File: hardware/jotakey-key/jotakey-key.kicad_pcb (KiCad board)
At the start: 2 copper layers, 18 x 47 mm, 27 parts, among them J1 USB_A_PCB_Edge, U1 STM32L432KCU6, U2 SLS32AIA010MH, U3 XC6206P332MR, U4 USBLC6-2SC6

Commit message: hardware: label the SWD pads, set the board finish
The five SWD test pads on the bottom get their signals in silkscreen
(DIO, CLK, RST, 3V3, GND), 0.8 mm high under each pad, placed by silk.py
from the test-point positions.

The stackup now records ENIG and a bevelled edge connector (set in
Board Setup > Board Finish), as HARDWARE.md specifies. The silkscreen
bolt on the touch electrode, lost when E1 was updated from a stale copy
of the library, is back. DRC: no violations.

Co-Authored-By: Claude Opus 5.5 <noreply@anthropic.com>
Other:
- board text added: "3V3"
- board text added: "CLK"
- board text added: "DIO"
- board text added: "GND"
- board text added: "RST"
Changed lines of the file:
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@@
 			(layer "F.SilkS"
 				(type "Top Silk Screen")
-				(color "White")
 			)
 			(layer "F.Paste"
@@
 			(layer "B.SilkS"
 				(type "Bottom Silk Screen")
-				(color "White")
 			)
-			(copper_finish "None")
+			(copper_finish "ENIG")
 			(dielectric_constraints no)
+			(edge_connector bevelled)
 		)
 		(pad_to_mask_clearance 0.05)
@@
 		(attr smd)
 		(duplicate_pad_numbers_are_jumpers no)
+		(fp_poly
+			(pts
+				(xy 0.3182 -3.5) (xy -2.5455 0.3182) (xy -0.6364 0.3182) (xy -1.9091 3.5) (xy 2.5455 -0.6364) (xy 0.3182 -0.6364)
+				(xy 2.2273 -3.5)
+			)
+			(stroke
+				(width 0)
+				(type solid)
+			)
+			(fill yes)
+			(layer "F.SilkS")
+		)
 		(fp_circle
 			(center 0 0)
@@
 		)
 		(embedded_fonts no)
-		(fp_poly (pts (xy 0.3182 -3.5000) (xy -2.5455 0.3182) (xy -0.6364 0.3182) (xy -1.9091 3.5000) (xy 2.5455 -0.6364) (xy 0.3182 -0.6364) (xy 2.2273 -3.5000)) (stroke (width 0) (type solid)) (fill yes) (layer "F.SilkS"))
 	)
 	(footprint "Capacitor_SMD:C_0402_1005Metric"
@@
 		)
 	)
+	(gr_text "DIO"
+		(at 94.92 99.65 0)
+		(layer "B.SilkS")
+		(effects
+			(font
+				(size 0.8 0.8)
+				(thickness 0.12)
+			)
+			(justify mirror)
+		)
+	)
+	(gr_text "CLK"
+		(at 97.46 99.65 0)
+		(layer "B.SilkS")
+		(effects
+			(font
+				(size 0.8 0.8)
+				(thickness 0.12)
+			)
+			(justify mirror)
+		)
+	)
+	(gr_text "RST"
+		(at 100 99.65 0)
+		(layer "B.SilkS")
+		(effects
+			(font
+				(size 0.8 0.8)
+				(thickness 0.12)
+			)
+			(justify mirror)
+		)
+	)
+	(gr_text "3V3"
+		(at 102.54 99.65 0)
+		(layer "B.SilkS")
+		(effects
+			(font
+				(size 0.8 0.8)
+				(thickness 0.12)
+			)
+			(justify mirror)
+		)
+	)
+	(gr_text "GND"
+		(at 105.08 99.65 0)
+		(layer "B.SilkS")
+		(effects
+			(font
+				(size 0.8 0.8)
+				(thickness 0.12)
+			)
+			(justify mirror)
+		)
+	)

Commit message: hardware: label the chips with their function
MCU, OPTIGA, LDO and ESD on the top silkscreen, 0.8 mm high, each in the
free space nearest its chip and clear of pads and pin-1 marks; silk.py
places them relative to the footprints. DRC: no violations.

Co-Authored-By: Claude Opus 5.5 <noreply@anthropic.com>
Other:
- board text added: "ESD"
- board text added: "LDO"
- board text added: "MCU"
- board text added: "OPTIGA"
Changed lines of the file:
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@@
+		)
+	)
+	(gr_text "LDO"
+		(at 95.5 82.95 0)
+		(layer "F.SilkS")
+		(effects
+			(font
+				(size 0.8 0.8)
+				(thickness 0.15)
+			)
+		)
+	)
+	(gr_text "ESD"
+		(at 100 87.6 0)
+		(layer "F.SilkS")
+		(effects
+			(font
+				(size 0.8 0.8)
+				(thickness 0.15)
+			)
+		)
+	)
+	(gr_text "MCU"
+		(at 100 99.5 0)
+		(layer "F.SilkS")
+		(effects
+			(font
+				(size 0.8 0.8)
+				(thickness 0.15)
+			)
+		)
+	)
+	(gr_text "OPTIGA"
+		(at 106.2 83 0)
+		(layer "F.SilkS")
+		(effects
+			(font
+				(size 0.8 0.8)
+				(thickness 0.15)
+			)
 		)
 	)

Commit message: Copyright notices, a release workflow, and nothing third-party
- (c) Javier Fernandez @ JotaSoft 2026 at the top of every source file
  (Rust, Lean, Python, Typst, shell), in the report's cover and page
  footers, on the board's bottom silkscreen, in the schematic and PCB
  title blocks, as the Cargo authors, and in a new README.
- .github/workflows/release.yml: on every hw-v*/fw-v* tag, build the
  report in its screen and print versions with a pinned Typst, keep both
  as workflow artifacts, and attach them to the tag's GitHub release.
- docs/fonts: the report's fonts (SIL OFL, and Bitstream Vera for the
  math font) with their licences, so local and CI builds match; the doc
  recipes build with them only.
- Third-party documents (datasheets, specifications, papers) are no
  longer tracked; their README indexes keep every source link.

Co-Authored-By: Claude Opus 5.5 <noreply@anthropic.com>
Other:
- board text added: "(c) Javier Fernandez @ JotaSoft 2026"
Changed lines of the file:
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@@
 		(comment 1 "Pin plan and parts: hardware/HARDWARE.md")
 		(comment 2 "Fabrication and assembly: JLCPCB, 2 layers, 2.0 mm, ENIG")
+		(comment 3 "(c) Javier Fernandez @ JotaSoft 2026")
 	)
 	(layers
@@
 			)
 			(justify mirror)
+		)
+	)
+	(gr_text "(c) Javier Fernandez\n@ JotaSoft 2026"
+		(at 100 110.6 0)
+		(layer "B.SilkS")
+		(effects
+			(font
+				(size 0.8 0.8)
+				(thickness 0.15)
+			)
+			(justify mirror)

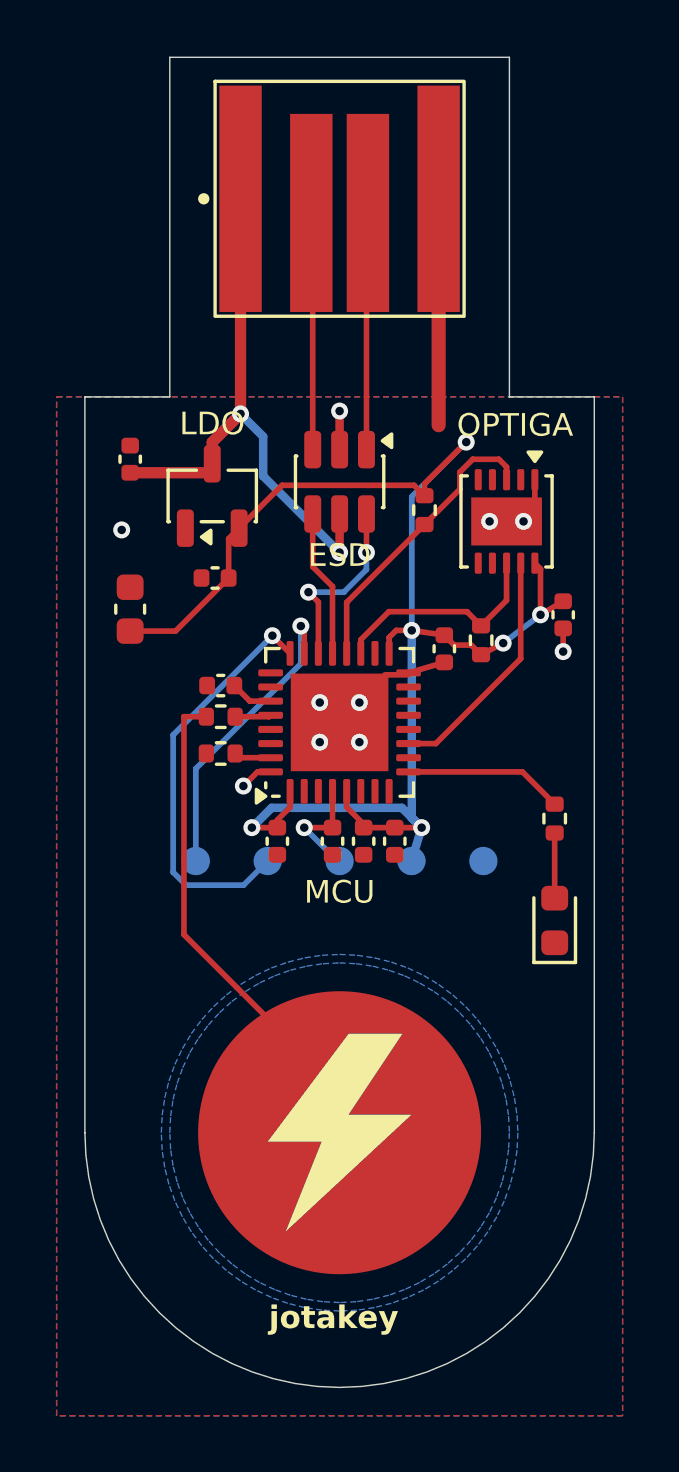
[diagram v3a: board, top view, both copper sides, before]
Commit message: hw: 0R bring-up links R6, R7; hardware 0.2.0
Split the 3.3 V supply into +3V3 (LDO), +3V3_MCU (via R6) and
+3V3_SE (via R7) so a hand-built board can be brought up one stage at
a time. The I2C pull-ups move to the OPTIGA's rail so they cannot
back-power it while R7 is open.

Board: R6 between the LDO and U4, R7 beside U4, R3 0.4 mm right, the
SE rail over U2 and down the edge to C9, a GND via to stitch the top
pour. ERC, DRC and schematic parity clean. HARDWARE.md, MANUFACTURING.md
(staged bring-up), README, chapter 7, renders and PDFs updated.

Co-Authored-By: Claude Opus 5.5 <noreply@anthropic.com>
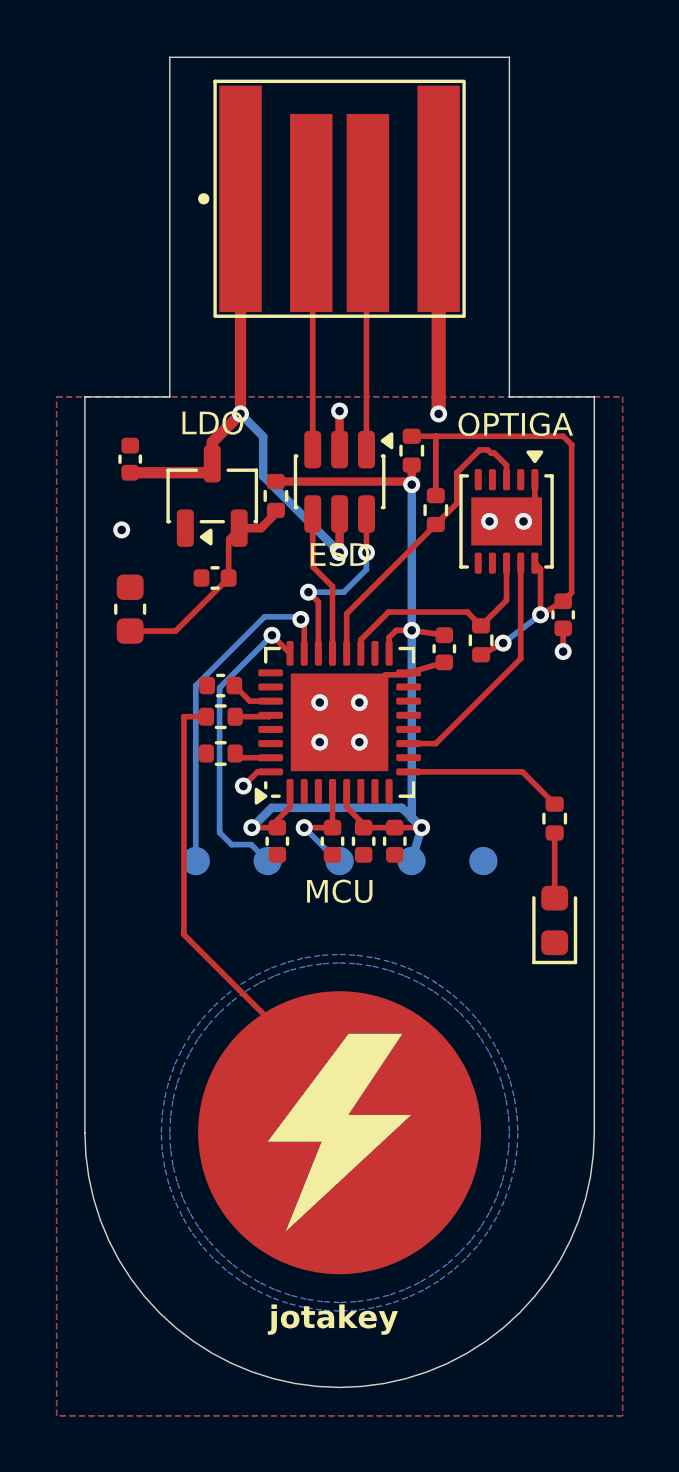
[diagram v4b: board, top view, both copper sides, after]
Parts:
- added R6: 0R, Resistor_SMD:R_0402_1005Metric, F.Cu at (97.8, 85.5)
- added R7: 0R, Resistor_SMD:R_0402_1005Metric, F.Cu at (102.5, 83.9)
- moved R3 0.40 mm to (103.4, 86.0)
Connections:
- C4 pad 1: +3V3 -> +3V3_MCU
- C5 pad 1: +3V3 -> +3V3_MCU
- C6 pad 1: +3V3 -> +3V3_MCU
- C7 pad 1: +3V3 -> +3V3_MCU
- C9 pad 1: +3V3 -> +3V3_SE
- R3 pad 1: +3V3 -> +3V3_SE
- R4 pad 1: +3V3 -> +3V3_SE
- TP4 pad 1: +3V3 -> +3V3_MCU
- U1 pad 1: +3V3 -> +3V3_MCU
- U1 pad 17: +3V3 -> +3V3_MCU
- U1 pad 5: +3V3 -> +3V3_MCU
- U2 pad 10: +3V3 -> +3V3_SE
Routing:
- net +3V3: track 53.9 -> 7.79 mm, vias 6 -> 0
- net +3V3_MCU: track 0.00 -> 34.2 mm, vias 0 -> 4
- net +3V3_SE: track 0.00 -> 18.9 mm, vias 0 -> 2
- net /SWCLK: track 14.6 -> 10.8 mm
- net /SWDIO: track 10.9 -> 12.2 mm
- net GND: track 10.9 -> 10.5 mm, vias 10 -> 11
